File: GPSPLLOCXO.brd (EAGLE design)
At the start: 73.7 x 52.5 mm, 26 parts, among them IC1 74AC14D, IC2 74LS86D, IC3 74LS390D, IC4 74LS390D, X1 5566-10

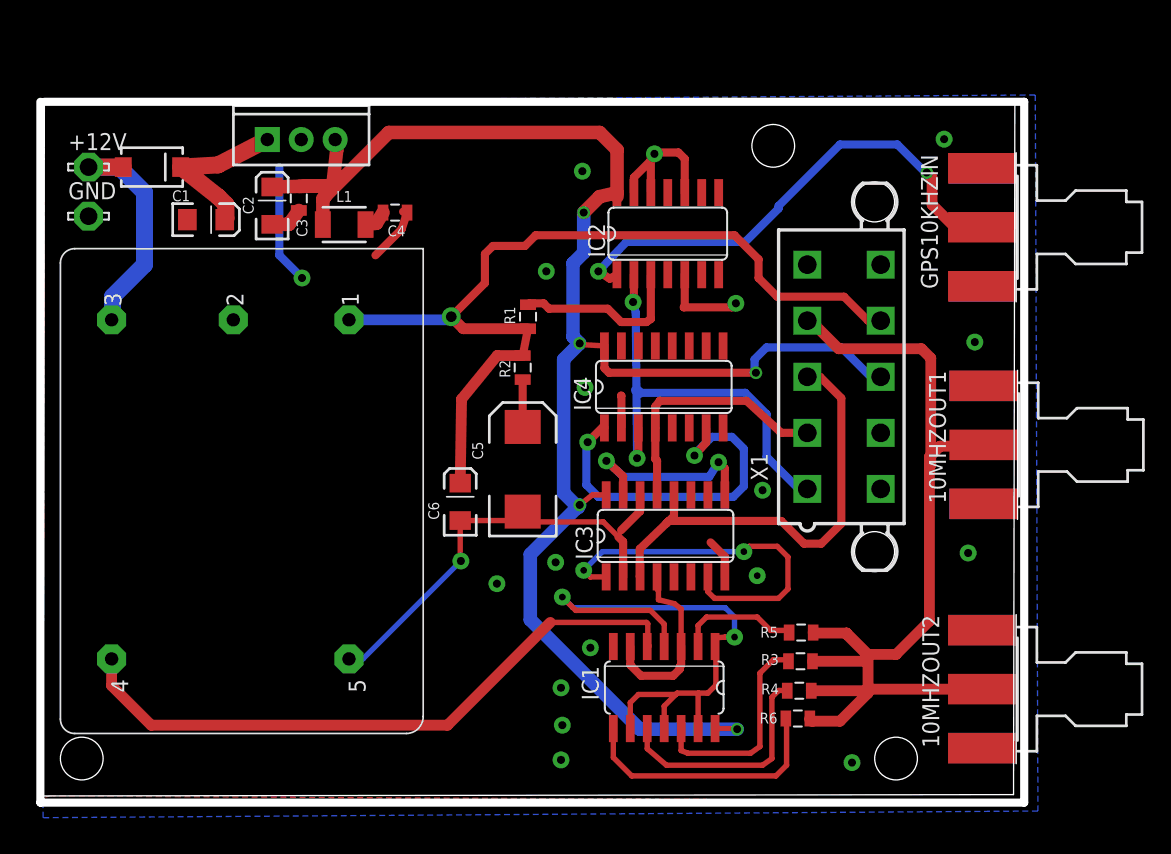
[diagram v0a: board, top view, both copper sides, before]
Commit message: Modified board to suite CNC/Milling
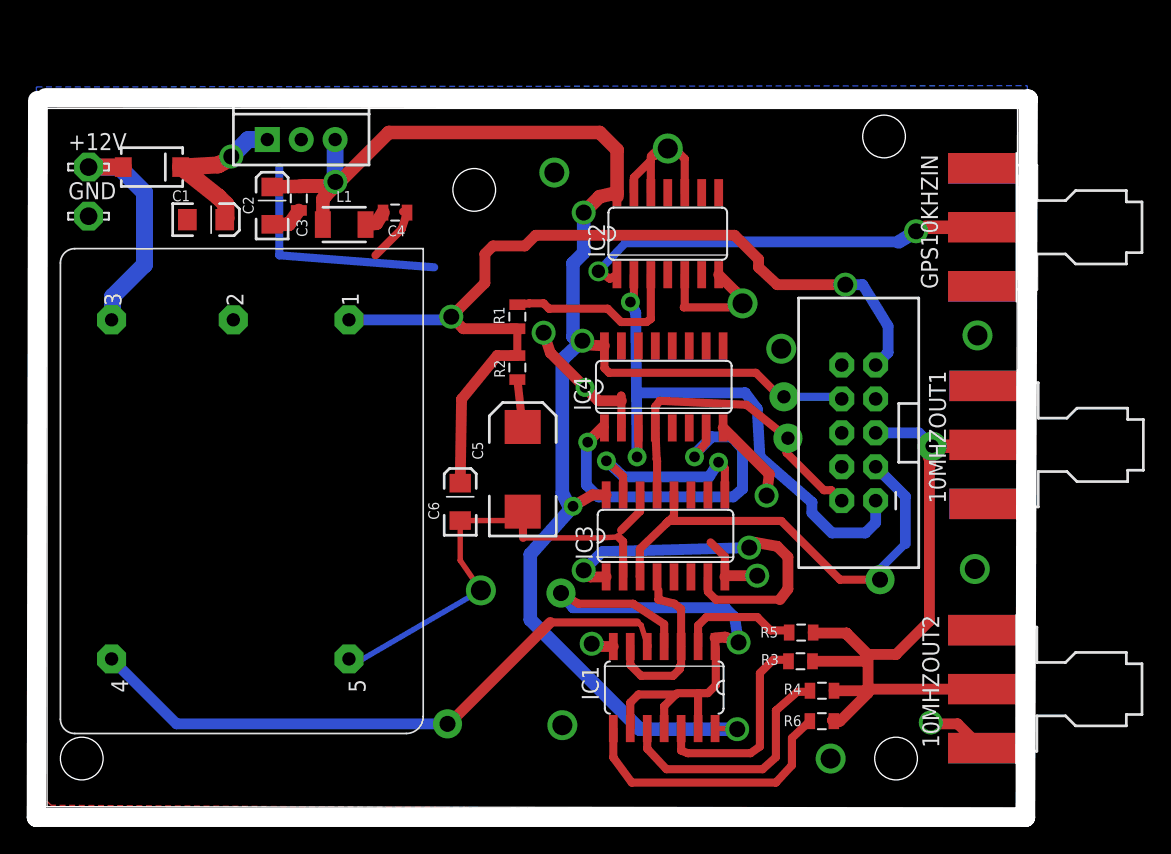
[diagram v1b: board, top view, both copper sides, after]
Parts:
- removed X1: 5566-10, con-molex:5566-10
- added JP1: M05X2SHD, SparkFun-Connectors:2X5-SHROUDED
- moved R6 1.81 mm to (58.4, 5.80)
- moved R4 1.70 mm to (58.5, 8.08)
- moved R1 0.80 mm to (35.6, 36.1)
- moved R2 0.40 mm to (35.6, 32.3)
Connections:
- net 100KHZ: now also JP1.2; no longer X1.2
- net 10KHZ: now also JP1.1; no longer X1.1
- net 10MHZ: now also JP1.5; no longer X1.4
- net 1MHZ: now also JP1.3; no longer X1.3
- net GND: now also JP1.10; no longer X1.10
- net VCC: now also JP1.8; no longer X1.8
- net VCOIN: now also JP1.9; no longer X1.9
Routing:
- net GND: track 73.7 -> 115.6 mm, vias 19 -> 15
- net 10MHZ: track 73.3 -> 56.8 mm, vias 0 -> 1
- net 10KHZ: track 34.2 -> 43.3 mm
- net 10KHZGPS: track 38.1 -> 32.4 mm
- net 100KHZ: track 19.2 -> 24.6 mm, vias 0 -> 1
- net VCC: track 128.8 -> 124.9 mm, vias 5 -> 6
- net VCOIN: track 68.0 -> 70.8 mm, vias 1 -> 2
- net N$6: track 48.3 -> 46.7 mm, vias 0 -> 1
- net N$15: track 19.6 -> 20.9 mm
- net N$17: track 17.4 -> 18.7 mm
- net N$14: track 44.7 -> 45.7 mm
- net 1MHZ: track 34.4 -> 35.3 mm, vias 0 -> 1
- net N$2: track 13.2 -> 14.0 mm
- net N$1: track 12.5 -> 12.8 mm, vias 0 -> 1
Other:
- board size 73.7 x 52.5 mm -> 74.3 x 53.9 mm

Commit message: Corrected FTDI mapping, added header to select power source.
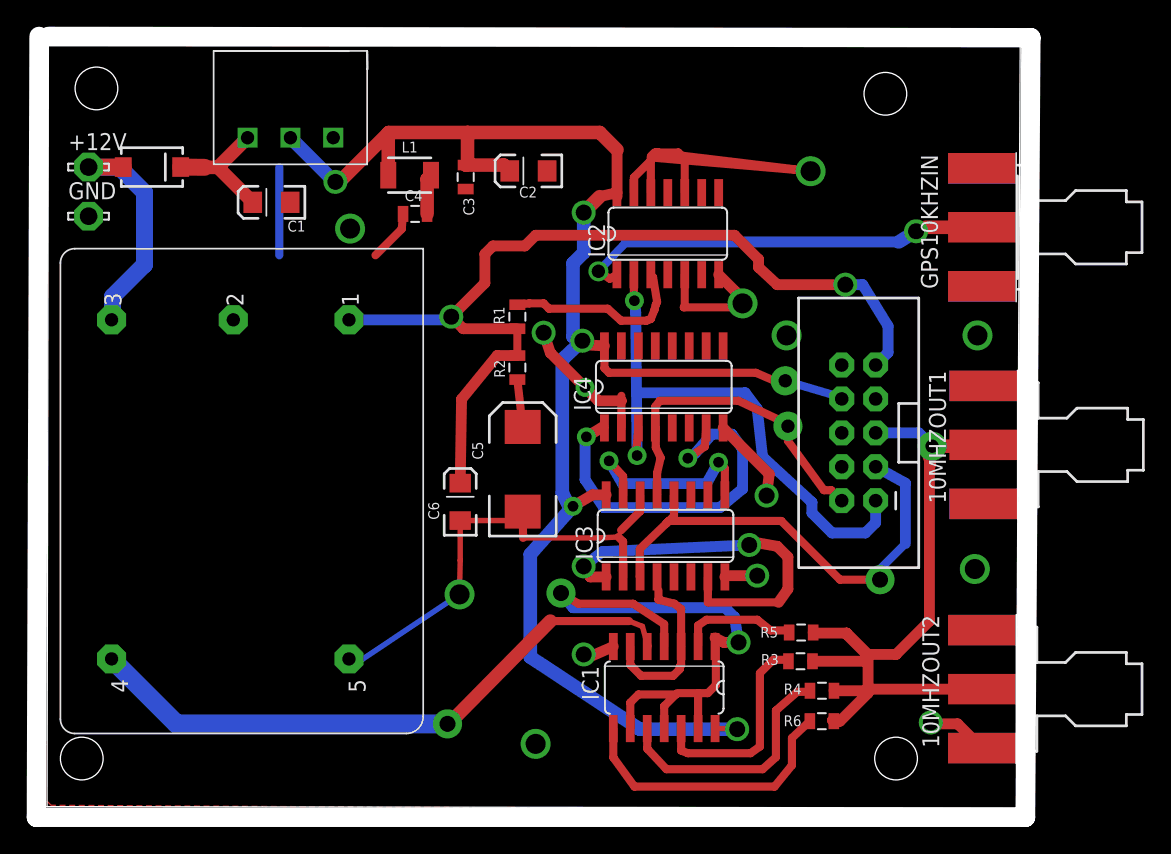
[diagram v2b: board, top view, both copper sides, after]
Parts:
- removed 7805: (no value), SparkFun-PowerIC:TO220-IGO
- added U$1: R-78HBXX-0.5R-78XX-0.5-SIP3, recom:SIP3
- moved C2 19.4 mm to (36.5, 47.0), turned to 180 degrees
- moved C3 12.6 mm to (31.8, 46.6)
- moved L1 6.14 mm to (27.6, 46.7)
- moved C1 5.07 mm to (17.2, 44.7), turned to 180 degrees
- moved C4 1.50 mm to (28.0, 43.8), turned to 180 degrees
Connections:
- net GND: now also U$1.+VIN; no longer 7805.GND
- net N$1: now also U$1.+VOUT; no longer 7805.IN
- net VCC: now also U$1.GND; no longer 7805.OUT
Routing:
- net N$1: track 12.8 -> 9.63 mm, vias 1 -> 0
- net GND: track 115.6 -> 118.1 mm, vias 15 -> 14
- net N$12: track 27.5 -> 29.6 mm
- net 100KHZ: track 24.6 -> 26.4 mm
- net U5+5: track 1.76 -> 3.02 mm
- net 10KHZ: track 43.3 -> 42.4 mm
- net N$8: track 28.4 -> 29.0 mm
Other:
- board size 74.3 x 53.9 mm -> 74.5 x 58.5 mm
